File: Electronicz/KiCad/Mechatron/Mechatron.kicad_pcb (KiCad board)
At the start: 2 copper layers, 28 parts, among them J1 ESP 32 L, J10 Ultra 4, J11 Ultra 5, J12 Ultra 6, J13 Ultra 7, J14 Ultra 8, J15 Battery, J16 LED1 Out, J17 LED3 Out, J18 LED3 Out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

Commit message: update schematic and create PCB
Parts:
- added R1: R, Resistor_THT:R_Axial_DIN0207_L6.3mm_D2.5mm_P10.16mm_Horizontal, F.Cu at (108.0, 101.6)
- added R2: R, Resistor_THT:R_Axial_DIN0207_L6.3mm_D2.5mm_P10.16mm_Horizontal, F.Cu at (100.3, 101.6)
- added R3: R, Resistor_THT:R_Axial_DIN0207_L6.3mm_D2.5mm_P10.16mm_Horizontal, F.Cu at (92.7, 101.6)
- moved Q1 127.2 mm to (81.3, 120.6), turned to 180 degrees
- moved Q7 8.45 mm to (111.8, 109.2)
- moved Q6 5.69 mm to (104.1, 109.2)
- moved J21 3.31 mm to (167.6, 66.0), turned to -90 degrees
- moved Q5 3.30 mm to (96.5, 109.2)
- moved J20 3.11 mm to (167.6, 71.1), turned to -90 degrees
- moved J19 2.96 mm to (167.6, 76.2), turned to -90 degrees
- moved J3 1.33 mm to (170.2, 81.3)
- moved J6 0.86 mm to (168.9, 96.5)
- moved J5 0.43 mm to (168.9, 91.4)
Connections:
- J10 pad 1: Net-(J1-Pin_2) -> Net-(J1-Pin_7)
- J10 pad 2: Net-(J1-Pin_7) -> Net-(J1-Pin_3)
- J10 pad 3: Net-(J1-Pin_3) -> Net-(J10-Pin_3)
- J10 pad 4: Net-(J10-Pin_4) -> Net-(J1-Pin_2)
- J11 pad 1: Net-(J1-Pin_2) -> Net-(J1-Pin_8)
- J11 pad 2: Net-(J1-Pin_8) -> Net-(J1-Pin_3)
- J11 pad 3: Net-(J1-Pin_3) -> Net-(J10-Pin_3)
- J11 pad 4: Net-(J10-Pin_4) -> Net-(J1-Pin_2)
- J12 pad 1: Net-(J1-Pin_2) -> Net-(J1-Pin_9)
- J12 pad 2: Net-(J1-Pin_9) -> Net-(J1-Pin_3)
- J12 pad 3: Net-(J1-Pin_3) -> Net-(J10-Pin_3)
- J12 pad 4: Net-(J10-Pin_4) -> Net-(J1-Pin_2)
- J13 pad 1: Net-(J1-Pin_2) -> Net-(J1-Pin_10)
- J13 pad 2: Net-(J1-Pin_10) -> Net-(J1-Pin_3)
- J13 pad 3: Net-(J1-Pin_3) -> Net-(J10-Pin_3)
- J13 pad 4: Net-(J10-Pin_4) -> Net-(J1-Pin_2)
- J14 pad 1: Net-(J1-Pin_2) -> Net-(J1-Pin_11)
- J14 pad 2: Net-(J1-Pin_11) -> Net-(J1-Pin_3)
- J14 pad 3: Net-(J1-Pin_3) -> Net-(J10-Pin_3)
- J14 pad 4: Net-(J10-Pin_4) -> Net-(J1-Pin_2)
- J19 pad 1: Net-(J1-Pin_2) -> Net-(J19-Pin_1)
- J19 pad 2: Net-(J19-Pin_2) -> Net-(J1-Pin_2)
- J2 pad 2: unconnected-(J2-Pin_2-Pad2) -> Net-(J1-Pin_2)
- J20 pad 1: Net-(J1-Pin_2) -> Net-(J20-Pin_1)
- J20 pad 2: Net-(J20-Pin_2) -> Net-(J1-Pin_2)
- J21 pad 1: Net-(J1-Pin_2) -> Net-(J21-Pin_1)
- J21 pad 2: Net-(J21-Pin_2) -> Net-(J1-Pin_2)
- J3 pad 2: Net-(J2-Pin_6) -> Net-(J1-Pin_2)
- J3 pad 3: Net-(J1-Pin_2) -> Net-(J2-Pin_6)
- J3 pad 4: Net-(J2-Pin_10) -> Net-(J2-Pin_7)
- J4 pad 2: Net-(J2-Pin_7) -> Net-(J1-Pin_2)
- J4 pad 3: Net-(J1-Pin_2) -> Net-(J2-Pin_8)
- J4 pad 4: Net-(J2-Pin_11) -> Net-(J2-Pin_9)
- J5 pad 2: Net-(J2-Pin_8) -> Net-(J1-Pin_2)
- J5 pad 3: Net-(J1-Pin_2) -> Net-(J2-Pin_10)
- J5 pad 4: Net-(J2-Pin_12) -> Net-(J2-Pin_11)
- J6 pad 2: Net-(J2-Pin_9) -> Net-(J1-Pin_2)
- J6 pad 3: Net-(J1-Pin_2) -> Net-(J2-Pin_12)
- J7 pad 1: Net-(J1-Pin_2) -> Net-(J1-Pin_4)
- J7 pad 2: Net-(J1-Pin_4) -> Net-(J1-Pin_3)
- J7 pad 3: Net-(J1-Pin_3) -> Net-(J10-Pin_3)
- J7 pad 4: Net-(J10-Pin_4) -> Net-(J1-Pin_2)
- J8 pad 1: Net-(J1-Pin_2) -> Net-(J1-Pin_5)
- J8 pad 2: Net-(J1-Pin_5) -> Net-(J1-Pin_3)
- J8 pad 3: Net-(J1-Pin_3) -> Net-(J10-Pin_3)
- J8 pad 4: Net-(J10-Pin_4) -> Net-(J1-Pin_2)
- J9 pad 1: Net-(J1-Pin_2) -> Net-(J1-Pin_6)
- J9 pad 2: Net-(J1-Pin_6) -> Net-(J1-Pin_3)
- J9 pad 3: Net-(J1-Pin_3) -> Net-(J10-Pin_3)
- J9 pad 4: Net-(J10-Pin_4) -> Net-(J1-Pin_2)
- Q1 pad 3: Net-(J10-Pin_4) -> Net-(J10-Pin_3)
- Q2 pad 3: Net-(J21-Pin_2) -> Net-(J21-Pin_1)
- Q3 pad 3: Net-(J20-Pin_2) -> Net-(J20-Pin_1)
- Q4 pad 3: Net-(J19-Pin_2) -> Net-(J19-Pin_1)
- Q5 pad 1: Net-(J10-Pin_4) -> Net-(J10-Pin_3)
- Q5 pad 2: Net-(J1-Pin_12) -> Net-(Q5-B)
- Q6 pad 1: Net-(J10-Pin_4) -> Net-(J10-Pin_3)
- Q6 pad 2: Net-(J1-Pin_13) -> Net-(Q6-B)
- Q7 pad 1: Net-(J10-Pin_4) -> Net-(J10-Pin_3)
- Q7 pad 2: Net-(J1-Pin_14) -> Net-(Q7-B)
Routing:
- net Net-(J1-Pin_2): track 0.00 -> 200.3 mm
- net Net-(J15-Pin_2): track 0.00 -> 183.0 mm
- net Net-(J10-Pin_3): track 0.00 -> 65.7 mm
- net Net-(J1-Pin_3): track 0.00 -> 64.0 mm
- net Net-(J2-Pin_6): track 0.00 -> 34.1 mm
- net Net-(J2-Pin_8): track 0.00 -> 32.8 mm
- net Net-(J2-Pin_10): track 0.00 -> 32.8 mm
- net Net-(J2-Pin_12): track 0.00 -> 32.8 mm
- net Net-(J2-Pin_3): track 0.00 -> 32.6 mm
- net Net-(J2-Pin_4): track 0.00 -> 31.5 mm
- net Net-(J2-Pin_7): track 0.00 -> 30.5 mm
- net Net-(J19-Pin_3): track 0.00 -> 30.5 mm
- net Net-(J2-Pin_9): track 0.00 -> 29.2 mm
- net Net-(J2-Pin_11): track 0.00 -> 29.2 mm
- net Net-(J2-Pin_13): track 0.00 -> 29.2 mm
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
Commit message: fix esp 32 pin distance
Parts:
- moved J19 7.62 mm to (175.2, 76.2)
- moved J20 7.62 mm to (175.2, 71.1)
- moved J21 7.62 mm to (175.2, 66.0)
- moved J3 7.62 mm to (177.8, 81.3)
- moved J4 7.62 mm to (176.5, 86.4)
- moved J5 7.62 mm to (176.5, 91.4)
- moved J6 7.62 mm to (176.5, 96.5)
- moved Q2 7.62 mm to (201.9, 66.9)
- moved Q3 7.62 mm to (201.9, 71.5)
- moved Q4 7.62 mm to (201.9, 76.2)
- moved J2 7.62 mm to (139.7, 66.0)
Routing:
- net Net-(J15-Pin_2): track 183.0 -> 190.6 mm

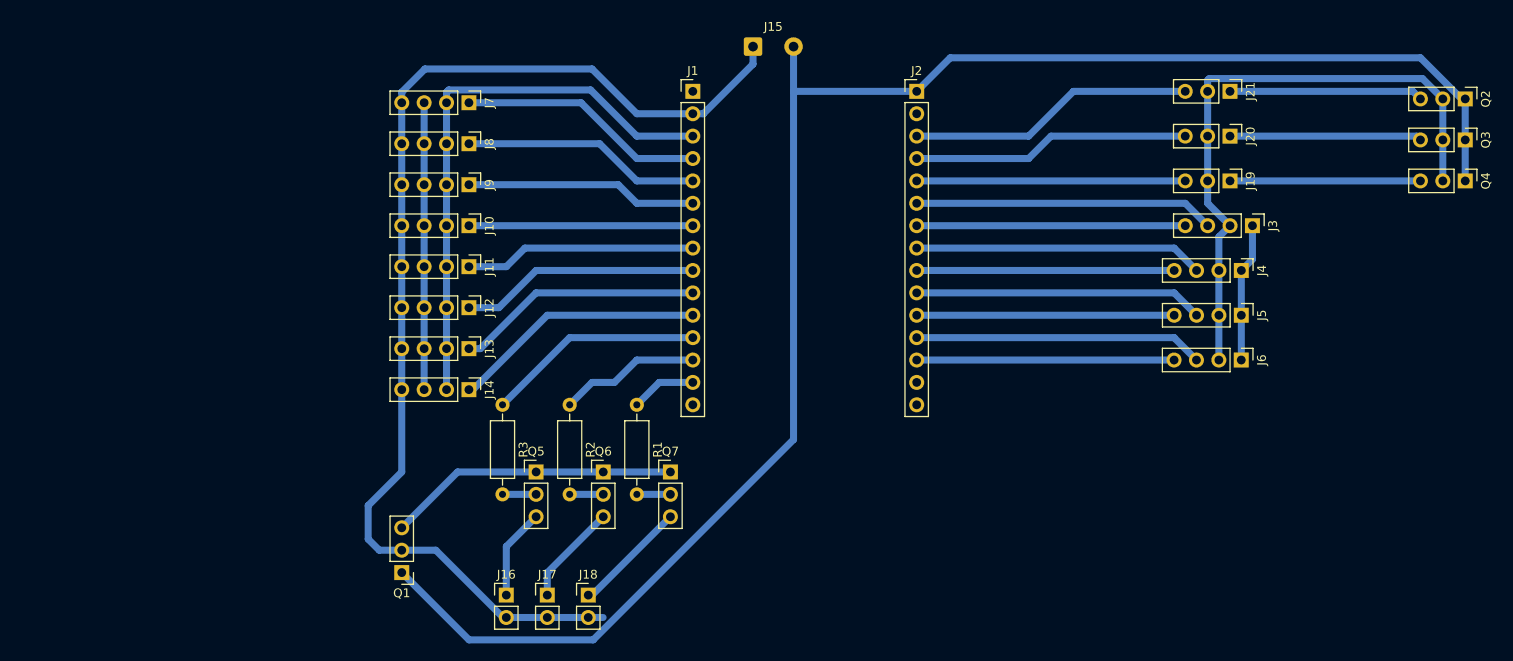
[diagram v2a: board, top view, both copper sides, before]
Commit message: change placement on the pcb
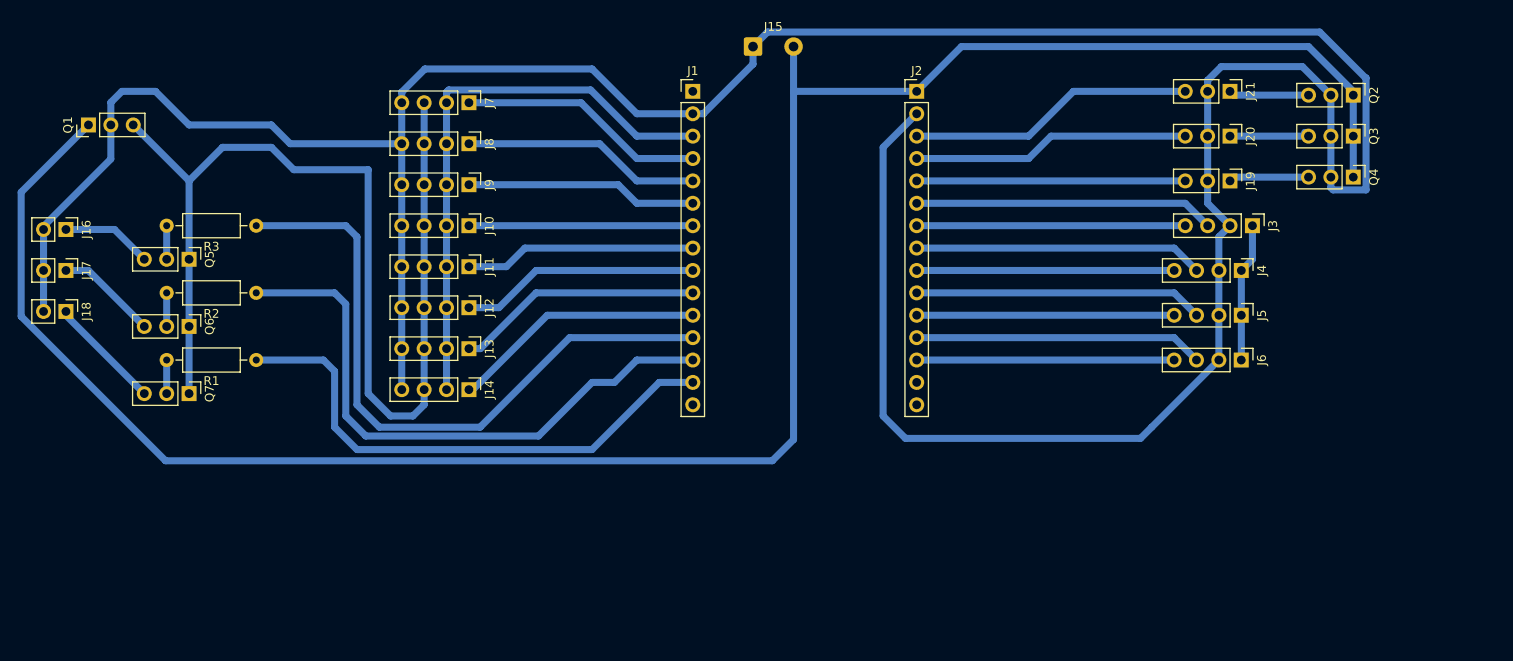
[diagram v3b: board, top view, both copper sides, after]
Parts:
- moved J18 67.4 mm to (43.2, 91.0), turned to -90 degrees
- moved J17 65.9 mm to (43.2, 86.4), turned to -90 degrees
- moved J16 64.9 mm to (43.2, 81.7), turned to -90 degrees
- moved Q1 62.0 mm to (45.7, 69.8), turned to 90 degrees
- moved Q7 55.3 mm to (57.1, 100.3), turned to -90 degrees
- moved Q6 49.8 mm to (57.1, 92.7), turned to -90 degrees
- moved Q5 46.2 mm to (57.1, 85.1), turned to -90 degrees
- moved R1 43.5 mm to (64.8, 96.5), turned to 180 degrees
- moved R2 37.8 mm to (64.8, 88.9), turned to 180 degrees
- moved R3 34.5 mm to (64.8, 81.3), turned to 180 degrees
- moved Q2 12.7 mm to (189.2, 66.5)
- moved Q3 12.7 mm to (189.2, 71.1)
- moved Q4 12.7 mm to (189.2, 75.8)
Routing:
- net Net-(J1-Pin_2): track 200.3 -> 371.6 mm
- net Net-(J10-Pin_3): track 65.7 -> 123.6 mm
- net Net-(J1-Pin_14): track 7.40 -> 60.6 mm
- net Net-(J15-Pin_2): track 190.6 -> 242.7 mm
- net Net-(J1-Pin_13): track 16.1 -> 67.3 mm
- net Net-(J1-Pin_12): track 24.7 -> 74.4 mm
- net Net-(J21-Pin_1): track 22.0 -> 9.08 mm
- net Net-(J19-Pin_1): track 21.6 -> 9.08 mm
- net Net-(J20-Pin_1): track 21.8 -> 9.51 mm
